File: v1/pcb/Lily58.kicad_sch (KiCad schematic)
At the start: 110 parts, among them P4 OLED, SW1 SW_PUSH, SW10 SW_PUSH, SW11 SW_PUSH, SW12 SW_PUSH, SW13 SW_PUSH, SW14 SW_PUSH, SW15 SW_PUSH, SW16 SW_PUSH, SW17 SW_PUSH, SW18 SW_PUSH, SW19 SW_PUSH, SW2 SW_PUSH, SW20 SW_PUSH, SW21 SW_PUSH, SW22 SW_PUSH, SW23 SW_PUSH, SW24 SW_PUSH, SW25 Rotary_Encoder_Switch, SW26 SW_PUSH, SW27 SW_PUSH, SW28 SW_PUSH, SW29 SW_PUSH, SW3 SW_PUSH, SW4 SW_PUSH, SW5 SW_PUSH, SW6 SW_PUSH, SW7 SW_PUSH, SW8 SW_PUSH, SW9 SW_PUSH, U1 NiceNano

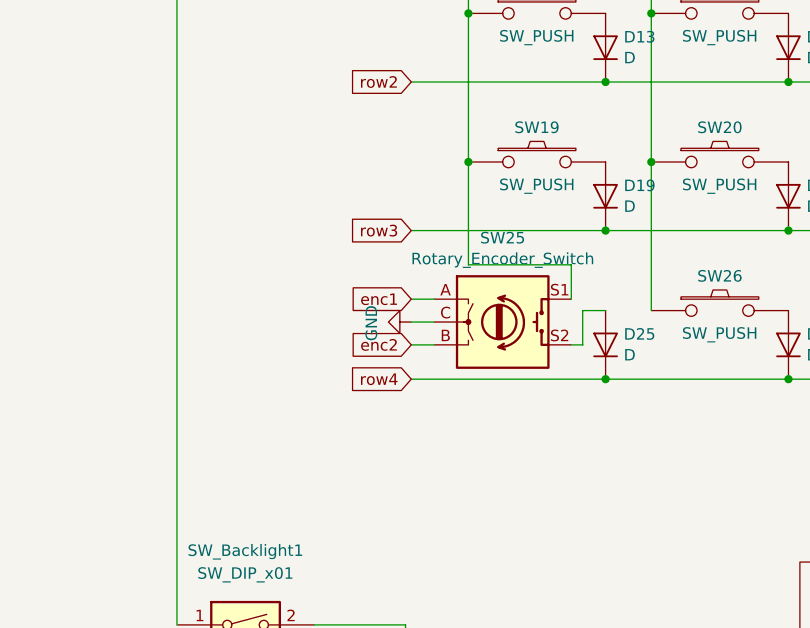
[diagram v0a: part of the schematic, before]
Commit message: Hopefully Fixed PCB
Added in the option to replace the right hand encoder with a switch, must be soldered though. Hopefully this PCB will work this time around!
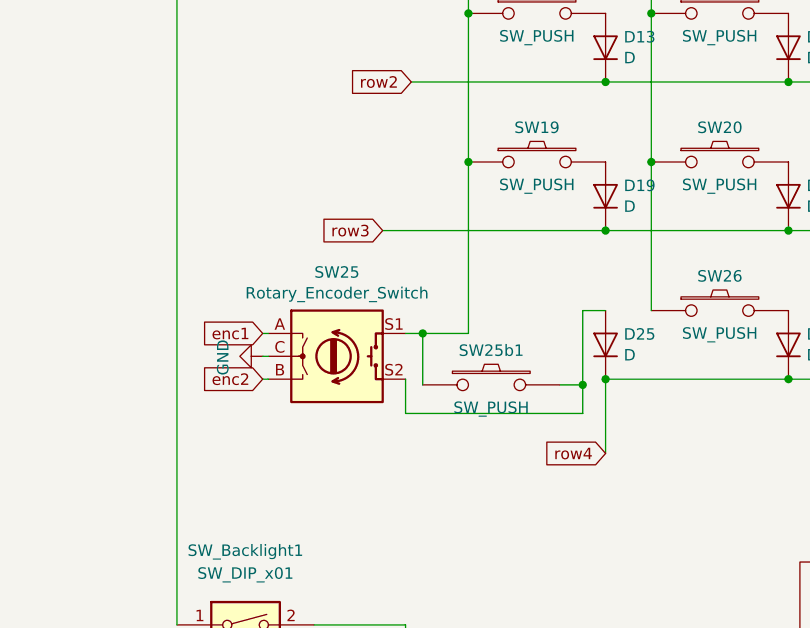
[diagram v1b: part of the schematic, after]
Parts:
- added SW25b1: SW_PUSH, Lily58-footprint:MX_Socket_18mm, symbol Lily58-rescue:SW_PUSH-Lily58-cache
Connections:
- net col5: now also SW25b1.1
- net at D25.2 (A), SW25.S2: now also SW25b1.2
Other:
- moved on the sheet: SW25
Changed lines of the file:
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@@
   (junction (at 102.87 60.96) (diameter 0) (color 0 0 0 0)
   )
+  (junction (at 139.7 106.68) (diameter 0) (color 0 0 0 0)
+  )
+  (junction (at 152.4 131.445) (diameter 0) (color 0 0 0 0)
+  )
   (junction (at 208.28 217.17) (diameter 0) (color 0 0 0 0)
   )
@@
   (junction (at 139.7 73.66) (diameter 0) (color 0 0 0 0)
   )
+  (junction (at 134.62 125.73) (diameter 0) (color 0 0 0 0)
+  )
   (junction (at 147.32 199.39) (diameter 0) (color 0 0 0 0)
   )
@@
   (junction (at 180.34 90.17) (diameter 0) (color 0 0 0 0)
   )
-  (junction (at 139.7 106.68) (diameter 0) (color 0 0 0 0)
-  )
   (junction (at 187.96 265.43) (diameter 0) (color 0 0 0 0)
   )
@@
     (stroke (width 0) (type default) (color 0 0 0 0))
   )
-  (wire (pts (xy 133.35 127) (xy 135.89 127))
+  (wire (pts (xy 116.84 130.81) (xy 117.475 130.81))
     (stroke (width 0) (type default) (color 0 0 0 0))
   )
@@
     (stroke (width 0) (type default) (color 0 0 0 0))
   )
-  (wire (pts (xy 133.35 130.81) (xy 154.94 130.81))
+  (wire (pts (xy 154.94 139.065) (xy 154.94 130.81))
     (stroke (width 0) (type default) (color 0 0 0 0))
   )
-  (wire (pts (xy 152.4 127) (xy 152.4 123.19))
+  (wire (pts (xy 152.4 123.19) (xy 152.4 131.445))
     (stroke (width 0) (type default) (color 0 0 0 0))
   )
@@
     (stroke (width 0) (type default) (color 0 0 0 0))
   )
-  (wire (pts (xy 139.7 106.68) (xy 139.7 118.11))
-    (stroke (width 0) (type default) (color 0 0 0 0))
-  )
   (wire (pts (xy 147.32 200.66) (xy 167.64 200.66))
     (stroke (width 0) (type default) (color 0 0 0 0))
@@
     (stroke (width 0) (type default) (color 0 0 0 0))
   )
-  (wire (pts (xy 154.94 114.3) (xy 133.35 114.3))
+  (wire (pts (xy 154.94 114.3) (xy 130.175 114.3))
     (stroke (width 0) (type default) (color 0 0 0 0))
   )
@@
     (stroke (width 0) (type default) (color 0 0 0 0))
   )
+  (wire (pts (xy 152.4 134.62) (xy 152.4 131.445))
+    (stroke (width 0) (type default) (color 0 0 0 0))
+  )
   (wire (pts (xy 236.22 97.79) (xy 256.54 97.79))
     (stroke (width 0) (type default) (color 0 0 0 0))
@@
     (stroke (width 0) (type default) (color 0 0 0 0))
   )
+  (wire (pts (xy 132.715 134.62) (xy 152.4 134.62))
+    (stroke (width 0) (type default) (color 0 0 0 0))
+  )
   (wire (pts (xy 236.22 64.77) (xy 256.54 64.77))
     (stroke (width 0) (type default) (color 0 0 0 0))
@@
     (stroke (width 0) (type default) (color 0 0 0 0))
   )
+  (wire (pts (xy 149.86 131.445) (xy 152.4 131.445))
+    (stroke (width 0) (type default) (color 0 0 0 0))
+  )
   (wire (pts (xy 167.64 200.66) (xy 187.96 200.66))
     (stroke (width 0) (type default) (color 0 0 0 0))
@@
     (stroke (width 0) (type default) (color 0 0 0 0))
   )
+  (wire (pts (xy 132.715 130.81) (xy 132.715 134.62))
+    (stroke (width 0) (type default) (color 0 0 0 0))
+  )
   (wire (pts (xy 208.28 233.68) (xy 228.6 233.68))
     (stroke (width 0) (type default) (color 0 0 0 0))
@@
     (stroke (width 0) (type default) (color 0 0 0 0))
   )
-  (wire (pts (xy 151.13 121.92) (xy 151.13 118.11))
-    (stroke (width 0) (type default) (color 0 0 0 0))
-  )
   (wire (pts (xy 175.26 130.81) (xy 195.58 130.81))
     (stroke (width 0) (type default) (color 0 0 0 0))
@@
     (stroke (width 0) (type default) (color 0 0 0 0))
   )
+  (wire (pts (xy 134.62 125.73) (xy 139.7 125.73))
+    (stroke (width 0) (type default) (color 0 0 0 0))
+  )
   (wire (pts (xy 147.32 250.19) (xy 167.64 250.19))
     (stroke (width 0) (type default) (color 0 0 0 0))
@@
     (stroke (width 0) (type default) (color 0 0 0 0))
   )
+  (wire (pts (xy 139.7 106.68) (xy 139.7 125.73))
+    (stroke (width 0) (type default) (color 0 0 0 0))
+  )
   (wire (pts (xy 167.64 250.19) (xy 187.96 250.19))
     (stroke (width 0) (type default) (color 0 0 0 0))
@@
     (stroke (width 0) (type default) (color 0 0 0 0))
   )
+  (wire (pts (xy 134.62 125.73) (xy 134.62 131.445))
+    (stroke (width 0) (type default) (color 0 0 0 0))
+  )
   (wire (pts (xy 154.94 130.81) (xy 175.26 130.81))
     (stroke (width 0) (type default) (color 0 0 0 0))
@@
     (stroke (width 0) (type default) (color 0 0 0 0))
   )
-  (wire (pts (xy 133.35 121.92) (xy 135.89 121.92))
-    (stroke (width 0) (type default) (color 0 0 0 0))
-  )
-  (wire (pts (xy 151.13 127) (xy 152.4 127))
+  (wire (pts (xy 116.84 125.73) (xy 117.475 125.73))
     (stroke (width 0) (type default) (color 0 0 0 0))
   )
@@
     (stroke (width 0) (type default) (color 0 0 0 0))
   )
+  (wire (pts (xy 134.62 125.73) (xy 132.715 125.73))
+    (stroke (width 0) (type default) (color 0 0 0 0))
+  )
   (wire (pts (xy 167.64 199.39) (xy 147.32 199.39))
     (stroke (width 0) (type default) (color 0 0 0 0))
@@
     (stroke (width 0) (type default) (color 0 0 0 0))
   )
-  (wire (pts (xy 151.13 118.11) (xy 139.7 118.11))
-    (stroke (width 0) (type default) (color 0 0 0 0))
-  )
   (wire (pts (xy 220.98 106.68) (xy 220.98 123.19))
     (stroke (width 0) (type default) (color 0 0 0 0))
@@
     (stroke (width 0) (type default) (color 0 0 0 0))
   )
-  (wire (pts (xy 133.35 124.46) (xy 135.89 124.46))
+  (wire (pts (xy 116.84 128.27) (xy 117.475 128.27))
     (stroke (width 0) (type default) (color 0 0 0 0))
   )
@@
     )
   )
-  (global_label "enc1" (shape input) (at 133.35 121.92 180) (fields_autoplaced)
+  (global_label "enc1" (shape input) (at 116.84 125.73 180) (fields_autoplaced)
     (effects (font (size 1.27 1.27)) (justify right))
-    (property "Intersheet References" "${INTERSHEET_REFS}" (id 0) (at 0 0 0)
+    (property "Intersheet References" "${INTERSHEET_REFS}" (id 0) (at -16.51 3.81 0)
       (effects (font (size 1.27 1.27)) hide)
     )
@@
     )
   )
-  (global_label "row4" (shape input) (at 133.35 130.81 180) (fields_autoplaced)
+  (global_label "row4" (shape input) (at 154.94 139.065 180) (fields_autoplaced)
     (effects (font (size 1.27 1.27)) (justify right))
-    (property "Intersheet References" "${INTERSHEET_REFS}" (id 0) (at 0 0 0)
+    (property "Intersheet References" "${INTERSHEET_REFS}" (id 0) (at 21.59 8.255 0)
       (effects (font (size 1.27 1.27)) hide)
     )
@@
     )
   )
-  (global_label "row3" (shape input) (at 133.35 114.3 180) (fields_autoplaced)
+  (global_label "row3" (shape input) (at 130.175 114.3 180) (fields_autoplaced)
     (effects (font (size 1.27 1.27)) (justify right))
-    (property "Intersheet References" "${INTERSHEET_REFS}" (id 0) (at 0 0 0)
+    (property "Intersheet References" "${INTERSHEET_REFS}" (id 0) (at -3.175 0 0)
       (effects (font (size 1.27 1.27)) hide)
     )
@@
     )
   )
-  (global_label "enc2" (shape input) (at 133.35 127 180) (fields_autoplaced)
+  (global_label "enc2" (shape input) (at 116.84 130.81 180) (fields_autoplaced)
     (effects (font (size 1.27 1.27)) (justify right))
-    (property "Intersheet References" "${INTERSHEET_REFS}" (id 0) (at 0 0 0)
+    (property "Intersheet References" "${INTERSHEET_REFS}" (id 0) (at -16.51 3.81 0)
       (effects (font (size 1.27 1.27)) hide)
     )
@@
     (pin "4")
   )
-  (symbol (lib_id "Device:Rotary_Encoder_Switch") (at 143.51 124.46 0) (unit 1)
+  (symbol (lib_id "Device:Rotary_Encoder_Switch") (at 125.095 128.27 0) (unit 1)
     (in_bom yes) (on_board yes)
-    (property "Reference" "SW25" (id 0) (at 143.51 115.1382 0))
-    (property "Value" "Rotary_Encoder_Switch" (id 1) (at 143.51 117.4496 0))
-    (property "Footprint" "Lily58-footprint:RotaryEncoder_Alps_EC11E-Switch_Vertical_H20mm" (id 2) (at 139.7 120.396 0)
+    (property "Reference" "SW25" (id 0) (at 125.095 118.9482 0))
+    (property "Value" "Rotary_Encoder_Switch" (id 1) (at 125.095 121.2596 0))
+    (property "Footprint" "Lily58-footprint:RotaryEncoder_Alps_EC11E-Switch_Vertical_H20mm" (id 2) (at 121.285 124.206 0)
       (effects (font (size 1.27 1.27)) hide)
     )
-    (property "Datasheet" "~" (id 3) (at 143.51 117.856 0)
+    (property "Datasheet" "~" (id 3) (at 125.095 121.666 0)
       (effects (font (size 1.27 1.27)) hide)
     )
@@
     (pin "S2")
   )
-  (symbol (lib_id "power:GND") (at 133.35 124.46 270) (unit 1)
+  (symbol (lib_id "power:GND") (at 116.84 128.27 270) (unit 1)
     (in_bom yes) (on_board yes)
-    (property "Reference" "#PWR0119" (id 0) (at 127 124.46 0)
+    (property "Reference" "#PWR0119" (id 0) (at 110.49 128.27 0)
       (effects (font (size 1.27 1.27)) hide)
     )
-    (property "Value" "GND" (id 1) (at 128.9558 124.587 0))
-    (property "Footprint" "" (id 2) (at 133.35 124.46 0)
+    (property "Value" "GND" (id 1) (at 112.4458 128.397 0))
+    (property "Footprint" "" (id 2) (at 116.84 128.27 0)
       (effects (font (size 1.27 1.27)) hide)
     )
-    (property "Datasheet" "" (id 3) (at 133.35 124.46 0)
+    (property "Datasheet" "" (id 3) (at 116.84 128.27 0)
       (effects (font (size 1.27 1.27)) hide)
     )
@@
     (pin "4")
   )
+  (symbol (lib_id "Lily58-rescue:SW_PUSH-Lily58-cache") (at 142.24 131.445 0) (unit 1)
+    (in_bom yes) (on_board yes)
+    (property "Reference" "SW25b1" (id 0) (at 142.24 127.635 0))
+    (property "Value" "SW_PUSH" (id 1) (at 142.24 133.985 0))
+    (property "Footprint" "Lily58-footprint:MX_Socket_18mm" (id 2) (at 142.24 131.445 0)
+      (effects (font (size 1.27 1.27)) hide)
+    )
+    (property "Datasheet" "" (id 3) (at 142.24 131.445 0))
+    (pin "1")
+    (pin "2")
+  )
   (symbol (lib_id "Connector:Conn_01x01_Male") (at 133.35 36.83 180) (unit 1)
     (in_bom yes) (on_board yes) (fields_autoplaced)
@@
       (reference "SW25") (unit 1) (value "Rotary_Encoder_Switch") (footprint "Lily58-footprint:RotaryEncoder_Alps_EC11E-Switch_Vertical_H20mm")
     )
+    (path "/1a5c491e-8024-4385-8baa-b821513dc78b"
+      (reference "SW25b1") (unit 1) (value "SW_PUSH") (footprint "Lily58-footprint:MX_Socket_18mm")
+    )
     (path "/00000000-0000-0000-0000-00005b722582"
